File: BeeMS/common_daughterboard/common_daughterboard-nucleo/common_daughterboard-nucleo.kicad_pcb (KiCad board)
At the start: 2 copper layers, 27 parts, among them J1 OUT_CONN, J2 TERM, J3 IN_CONN, J4 HEAD, J5 TAIL, J6 Conn_02x10_Odd_Even, Q1 BSS138, Q2 BSS138, U1 MCP2558FD-xSN

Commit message: BeeMS Common Daughterboard V0.0.1
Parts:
- added C5: 47uF, Capacitor_SMD:C_1210_3225Metric_Pad1.42x2.65mm_HandSolder, F.Cu at (119.9, 109.8)
- added svg2mod: G***, BeeMS:Half-U-Half-car-thresh, B.Cu at (119.9, 111.3)
- moved J3 1.47 mm to (131.6, 108.4)
- moved J1 0.83 mm to (108.5, 115.7)
- moved RN1 0.69 mm to (114.8, 134.6)
- moved R5 0.31 mm to (103.3, 123.1)
- moved Q2 0.27 mm to (130.0, 129.0), turned to 0 degrees
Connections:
- Q2 pad 2: Net-(C1-Pad1) -> Net-(Q2-Pad2)
- Q2 pad 3: Net-(Q2-Pad3) -> Net-(C1-Pad1)
- R2 pad 1: Net-(Q2-Pad3) -> Net-(Q2-Pad2)
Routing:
- net +12V: track 0.00 -> 98.3 mm
- net +3V3: track 5.59 -> 101.6 mm, vias 0 -> 4
- net +5V: track 0.00 -> 57.8 mm, vias 0 -> 2
- net I2C2_SCL: track 15.6 -> 42.7 mm, vias 0 -> 2
- net I2C1_SCL: track 32.2 -> 46.6 mm, vias 4 -> 0
- net Net-(A1-Pad11): track 22.4 -> 36.7 mm, vias 0 -> 1
- net A3: track 10.0 -> 21.9 mm, vias 1 -> 0
- net CAN_-: track 41.8 -> 48.3 mm, vias 0 -> 3
- net NBR_OUT: track 66.9 -> 72.9 mm
- net Net-(Q2-Pad2): track 0.00 -> 4.71 mm
- net Net-(Q2-Pad3): track 4.20 -> 0.00 mm
- net Net-(J2-Pad1): track 32.6 -> 29.9 mm
- net CAN_+: track 48.9 -> 51.3 mm, vias 4 -> 5
- net D0: track 13.9 -> 11.7 mm, vias 1 -> 0
- net GND: track 0.00 -> 1.90 mm, vias 0 -> 10
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- added copper zone on B.Cu, net GND
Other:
- board outline added: 45.2 x 65 mm
- board text added: "BeeMS Common Mezzanine (V0.0.1)"

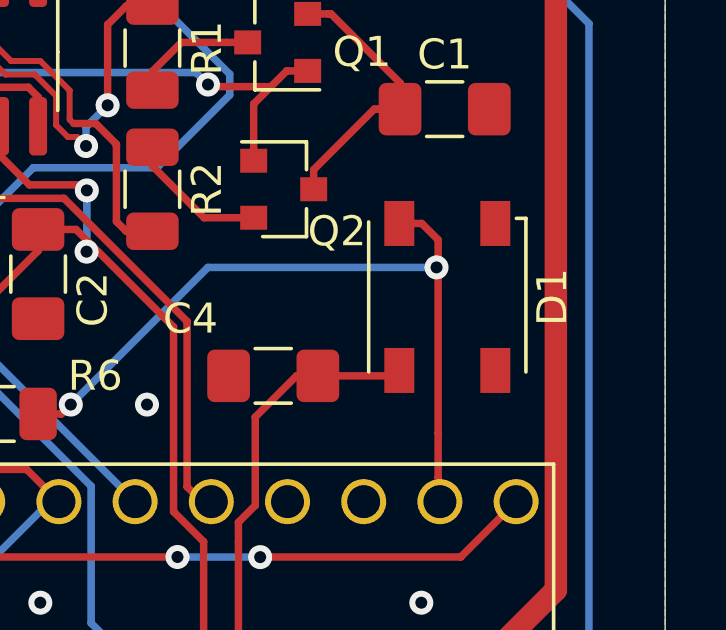
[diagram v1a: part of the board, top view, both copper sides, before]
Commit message: Added BOM for the nucleo common daughterboard
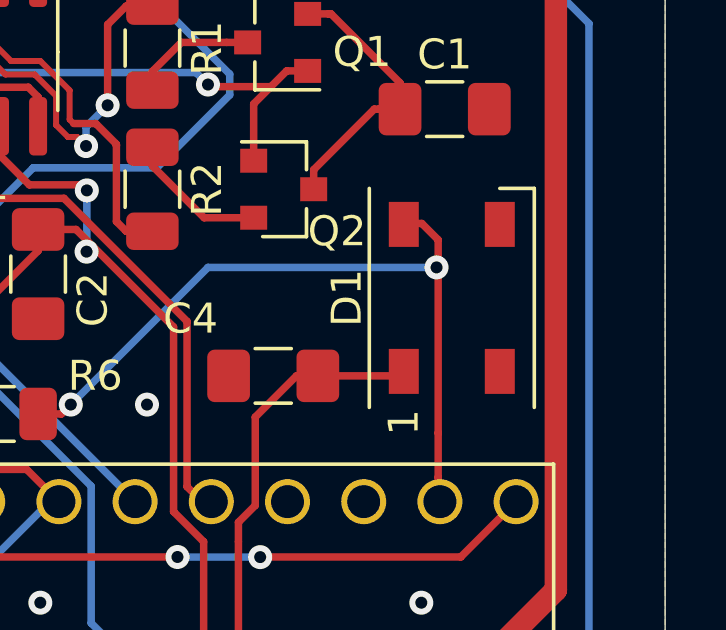
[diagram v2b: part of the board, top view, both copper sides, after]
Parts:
- C1: value 4700pF -> 4.7nF
- C2, C3: value .1uF -> 0.1uF
- D1: value Inolux_IN-PI554FCH -> WS2812B; footprint LED_SMD:LED_Inolux_IN-PI554FCH_PLCC4_5.0x5.0mm_P3.2mm -> LED_SMD:LED_WS2812B_PLCC4_5.0x5.0mm_P3.2mm
- H1: value TL -> G
- H2: value BL -> G
- H3: value BR -> G
- H4: value TR -> G
- moved D1 0.15 mm to (135.6, 132.6), turned to 90 degrees
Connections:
- D1 pad 1: GND -> +5V
- D1 pad 2: Net-(A1-Pad2) -> Net-(D1-Pad2)
- D1 pad 3: +5V -> GND
- D1 pad 4: Net-(D1-Pad4) -> Net-(A1-Pad2)
